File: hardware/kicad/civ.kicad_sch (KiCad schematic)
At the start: 3 parts, among them J1 CIV_3.5mm_Jack_TipRingSleeve, Q1 2N7000

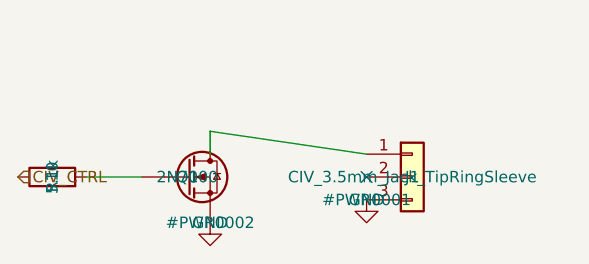
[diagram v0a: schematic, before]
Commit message: fix: repair schematic connectivity, real MAX3421E pinout, footprint assignment
- Root sheet pins were placed outside the sheet boxes, so no cross-sheet
  net (IO5->CI-V, USB D+/D-, SPI, VBUS_5V, 5V_HOST) was actually connected.
  Rebuilt pins on the sheet borders with wire stubs + labels.
- MCU: SW1/SW2 pin 2 carried both GND and EN/BOOT0 (short to ground);
  GND moved to pin 1. Unused ESP32 GPIOs marked no-connect.
- USB_Host rebuilt around the real MAX3421E TQFN-32 pinout (datasheet
  19-3953): 33 ohm D+/D- series resistors, 1uF VCC/VBCOMP, 0.1uF VL.
- J1 now AudioJack3 (T/R/S) with CUI SJ1-3523N footprint; Q1 is a real
  2N7000 (TO-92).
- PWR_FLAGs added; ERC (raw kicad-cli) has 0 errors.
- Board outline 65x45 mm, 54 footprints assigned and written to symbol
  Footprint fields, netlist applied. Placement is a rough grid only; no
  routing yet.
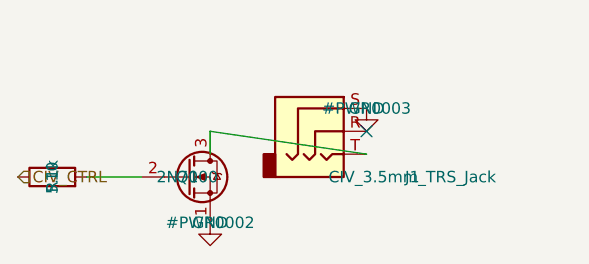
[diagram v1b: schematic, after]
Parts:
- removed J1: CIV_3.5mm_Jack_TipRingSleeve, symbol Connector_Generic:Conn_01x03
- removed Q1: 2N7000, symbol Device:Q_NMOS
- added J1: CIV_3.5mm_TRS_Jack, Connector_Audio:Jack_3.5mm_CUI_SJ1-3523N_Horizontal, symbol Connector_Audio:AudioJack3
- added Q1: 2N7000, Package_TO_SOT_THT:TO-92_Inline, symbol Transistor_FET:2N7000
- R10: footprint (none) -> Resistor_SMD:R_0603_1608Metric
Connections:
- net GND: now also J1.S, Q1.1 (S)
- net at R10.2: now also Q1.2 (G)
- new net: J1.T, Q1.3 (D)
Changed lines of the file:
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@@
 	(embedded_fonts no)
-	(symbol
-		(lib_id "Connector_Generic:Conn_01x03")
-		(at 70 110 0)
-		(unit 1)
-		(exclude_from_sim no)
-		(in_bom yes)
-		(on_board yes)
-		(dnp no)
-		(property "Reference" "J1"
-			(at 70 110 0)
-			(effects
-				(font
-					(size 1.27 1.27)
-				)
-			)
-		)
-		(property "Value" "CIV_3.5mm_Jack_TipRingSleeve"
-			(at 70 110 0)
-			(effects
-				(font
-					(size 1.27 1.27)
-				)
-			)
-		)
-		(property "Footprint" ""
-			(at 70 110 0)
-			(effects
-				(font
-					(size 1.27 1.27)
-				)
-				(hide yes)
-			)
-		)
-		(property "Datasheet" ""
-			(at 70 110 0)
-			(effects
-				(font
-					(size 1.27 1.27)
-				)
-				(hide yes)
-			)
-		)
-		(property "Description" "Generic connector, single row, 01x03, script generated (kicad-library-utils/schlib/autogen/connector/)"
-			(at 70 110 0)
-			(effects
-				(font
-					(size 1.27 1.27)
-				)
-				(hide yes)
-			)
-		)
-		(pin "1"
-		)
-		(pin "2"
-		)
-		(pin "3"
-		)
-		(instances
-			(project "WaveRig"
-				(path "/840e083b-e0fc-4c92-9ef6-5f402d7ae31c/890b54cb-1ed8-4869-b127-85ce65e524b6"
-					(reference "J1")
-					(unit 1)
-				)
-			)
-		)
-	)
-	(symbol
-		(lib_id "Device:Q_NMOS")
-		(at 45 110 0)
-		(unit 1)
-		(exclude_from_sim no)
-		(in_bom yes)
-		(on_board yes)
-		(dnp no)
-		(property "Reference" "Q1"
-			(at 45 110 0)
-			(effects
-				(font
-					(size 1.27 1.27)
-				)
-			)
-		)
-		(property "Value" "2N7000"
-			(at 45 110 0)
-			(effects
-				(font
-					(size 1.27 1.27)
-				)
-			)
-		)
-		(property "Footprint" ""
-			(at 45 110 0)
-			(effects
-				(font
-					(size 1.27 1.27)
-				)
-				(hide yes)
-			)
-		)
-		(property "Datasheet" ""
-			(at 45 110 0)
-			(effects
-				(font
-					(size 1.27 1.27)
-				)
-				(hide yes)
-			)
-		)
-		(property "Description" "N-MOSFET transistor"
-			(at 45 110 0)
-			(effects
-				(font
-					(size 1.27 1.27)
-				)
-				(hide yes)
-			)
-		)
-		(pin "D"
-		)
-		(pin "G"
-		)
-		(pin "S"
-		)
-		(instances
-			(project "WaveRig"
-				(path "/840e083b-e0fc-4c92-9ef6-5f402d7ae31c/890b54cb-1ed8-4869-b127-85ce65e524b6"
-					(reference "Q1")
-					(unit 1)
-				)
-			)
-		)
-	)
 	(symbol
 		(lib_id "Device:R")
@@
 			)
 		)
-		(property "Footprint" ""
+		(property "Footprint" "Resistor_SMD:R_0603_1608Metric"
 			(at 30 110 0)
 			(effects
@@
 			(width 0)
 			(type default)
-		)
-	)
-	(no_connect
-		(at 64.92 110)
-	)
-	(symbol
-		(lib_id "power:GND")
-		(at 64.92 112.54 0)
-		(unit 1)
-		(exclude_from_sim no)
-		(in_bom yes)
-		(on_board yes)
-		(dnp no)
-		(property "Reference" "#PWR0001"
-			(at 64.92 112.54 0)
-			(effects
-				(font
-					(size 1.27 1.27)
-				)
-			)
-		)
-		(property "Value" "GND"
-			(at 64.92 112.54 0)
-			(effects
-				(font
-					(size 1.27 1.27)
-				)
-			)
-		)
-		(property "Footprint" ""
-			(at 64.92 112.54 0)
-			(effects
-				(font
-					(size 1.27 1.27)
-				)
-				(hide yes)
-			)
-		)
-		(property "Datasheet" ""
-			(at 64.92 112.54 0)
-			(effects
-				(font
-					(size 1.27 1.27)
-				)
-				(hide yes)
-			)
-		)
-		(property "Description" "Power symbol creates a global label with name \"GND\" , ground"
-			(at 64.92 112.54 0)
-			(effects
-				(font
-					(size 1.27 1.27)
-				)
-				(hide yes)
-			)
-		)
-		(pin "1"
-		)
-		(instances
-			(project "WaveRig"
-				(path "/840e083b-e0fc-4c92-9ef6-5f402d7ae31c/890b54cb-1ed8-4869-b127-85ce65e524b6"
-					(reference "#PWR0001")
-					(unit 1)
-				)
-			)
 		)
 	)
@@
 		)
 	)
+	(symbol
+		(lib_id "Transistor_FET:2N7000")
+		(at 45 110 0)
+		(unit 1)
+		(exclude_from_sim no)
+		(in_bom yes)
+		(on_board yes)
+		(dnp no)
+		(property "Reference" "Q1"
+			(at 45 110 0)
+			(effects
+				(font
+					(size 1.27 1.27)
+				)
+			)
+		)
+		(property "Value" "2N7000"
+			(at 45 110 0)
+			(effects
+				(font
+					(size 1.27 1.27)
+				)
+			)
+		)
+		(property "Footprint" "Package_TO_SOT_THT:TO-92_Inline"
+			(at 45 110 0)
+			(effects
+				(font
+					(size 1.27 1.27)
+				)
+				(hide yes)
+			)
+		)
+		(property "Datasheet" "https://www.vishay.com/docs/70226/70226.pdf"
+			(at 45 110 0)
+			(effects
+				(font
+					(size 1.27 1.27)
+				)
+				(hide yes)
+			)
+		)
+		(property "Description" "0.2A Id, 200V Vds, N-Channel MOSFET, 2.6V Logic Level, TO-92"
+			(at 45 110 0)
+			(effects
+				(font
+					(size 1.27 1.27)
+				)
+				(hide yes)
+			)
+		)
+		(pin "1"
+		)
+		(pin "2"
+		)
+		(pin "3"
+		)
+		(instances
+			(project "WaveRig"
+				(path "/840e083b-e0fc-4c92-9ef6-5f402d7ae31c/890b54cb-1ed8-4869-b127-85ce65e524b6"
+					(reference "Q1")
+					(unit 1)
+				)
+			)
+		)
+	)
+	(symbol
+		(lib_id "Connector_Audio:AudioJack3")
+		(at 59.84 104.92 0)
+		(unit 1)
+		(exclude_from_sim no)
+		(in_bom yes)
+		(on_board yes)
+		(dnp no)
+		(property "Reference" "J1"
+			(at 70 110 0)
+			(effects
+				(font
+					(size 1.27 1.27)
+				)
+			)
+		)
+		(property "Value" "CIV_3.5mm_TRS_Jack"
+			(at 70 110 0)
+			(effects
+				(font
+					(size 1.27 1.27)
+				)
+			)
+		)
+		(property "Footprint" "Connector_Audio:Jack_3.5mm_CUI_SJ1-3523N_Horizontal"
+			(at 70 110 0)
+			(effects
+				(font
+					(size 1.27 1.27)
+				)
+				(hide yes)
+			)
+		)
+		(property "Datasheet" ""
+			(at 70 110 0)
+			(effects
+				(font
+					(size 1.27 1.27)
+				)
+				(hide yes)
+			)
+		)
+		(property "Description" "Audio Jack, 3 Poles (Stereo / TRS)"
+			(at 70 110 0)
+			(effects
+				(font
+					(size 1.27 1.27)
+				)
+				(hide yes)
+			)
+		)
+		(pin "R"
+		)
+		(pin "S"
+		)
+		(pin "T"
+		)
+		(instances
+			(project "WaveRig"
+				(path "/840e083b-e0fc-4c92-9ef6-5f402d7ae31c/890b54cb-1ed8-4869-b127-85ce65e524b6"
+					(reference "J1")
+					(unit 1)
+				)
+			)
+		)
+	)
+	(symbol
+		(lib_id "power:GND")
+		(at 64.92 102.38 0)
+		(unit 1)
+		(exclude_from_sim no)
+		(in_bom yes)
+		(on_board yes)
+		(dnp no)
+		(property "Reference" "#PWR0003"
+			(at 64.92 102.38 0)
+			(effects
+				(font
+					(size 1.27 1.27)
+				)
+			)
+		)
+		(property "Value" "GND"
+			(at 64.92 102.38 0)
+			(effects
+				(font
+					(size 1.27 1.27)
+				)
+			)
+		)
+		(property "Footprint" ""
+			(at 64.92 102.38 0)
+			(effects
+				(font
+					(size 1.27 1.27)
+				)
+				(hide yes)
+			)
+		)
+		(property "Datasheet" ""
+			(at 64.92 102.38 0)
+			(effects
+				(font
+					(size 1.27 1.27)
+				)
+				(hide yes)
+			)
+		)
+		(property "Description" "Power symbol creates a global label with name \"GND\" , ground"
+			(at 64.92 102.38 0)
+			(effects
+				(font
+					(size 1.27 1.27)
+				)
+				(hide yes)
+			)
+		)
+		(pin "1"
+		)
+		(instances
+			(project "WaveRig"
+				(path "/840e083b-e0fc-4c92-9ef6-5f402d7ae31c/890b54cb-1ed8-4869-b127-85ce65e524b6"
+					(reference "#PWR0003")
+					(unit 1)
+				)
+			)
+		)
+	)
+	(no_connect
+		(at 64.92 104.92)
+	)
 )

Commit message: fix: datasheet audit - correct charger pinout, LDO for 3V3, DW01A/FS8205A, MAX3232, CI-V RX
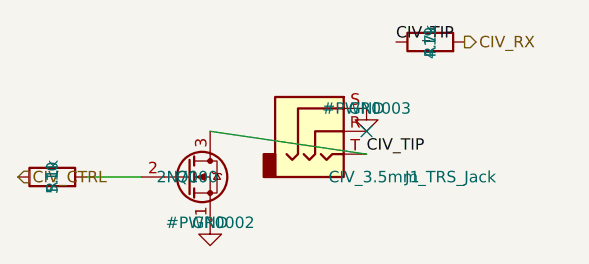
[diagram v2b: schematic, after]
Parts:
- added R19: 4.7k, Resistor_SMD:R_0603_1608Metric, symbol Device:R
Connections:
- net CIV_TIP: now reaches J1.T, Q1.3 (D)
- net CIV_TIP: now also R19.1
- new net CIV_RX: R19.2
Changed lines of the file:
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@@
-	(wire
-		(pts
-			(xy 47.54 104.92)
-			(xy 47.54 107.46)
-		)
-		(stroke
-			(width 0)
-			(type default)
-		)
-	)
 	(wire
 		(pts
@@
 		(at 64.92 104.92)
 	)
+	(symbol
+		(lib_id "Device:R")
+		(at 72 95 90)
+		(unit 1)
+		(exclude_from_sim no)
+		(in_bom yes)
+		(on_board yes)
+		(dnp no)
+		(property "Reference" "R19"
+			(at 72 95 0)
+			(effects
+				(font
+					(size 1.27 1.27)
+				)
+			)
+		)
+		(property "Value" "4.7k"
+			(at 72 95 0)
+			(effects
+				(font
+					(size 1.27 1.27)
+				)
+			)
+		)
+		(property "Footprint" "Resistor_SMD:R_0603_1608Metric"
+			(at 72 95 0)
+			(effects
+				(font
+					(size 1.27 1.27)
+				)
+				(hide yes)
+			)
+		)
+		(property "Datasheet" ""
+			(at 72 95 0)
+			(effects
+				(font
+					(size 1.27 1.27)
+				)
+				(hide yes)
+			)
+		)
+		(property "Description" "Resistor"
+			(at 72 95 0)
+			(effects
+				(font
+					(size 1.27 1.27)
+				)
+				(hide yes)
+			)
+		)
+		(pin "1"
+		)
+		(pin "2"
+		)
+		(instances
+			(project "WaveRig"
+				(path "/840e083b-e0fc-4c92-9ef6-5f402d7ae31c/890b54cb-1ed8-4869-b127-85ce65e524b6"
+					(reference "R19")
+					(unit 1)
+				)
+			)
+		)
+	)
+	(label "CIV_TIP"
+		(at 64.92 107.46 0)
+		(effects
+			(font
+				(size 1.27 1.27)
+			)
+			(justify left bottom)
+		)
+	)
+	(label "CIV_TIP"
+		(at 68.19 95 0)
+		(effects
+			(font
+				(size 1.27 1.27)
+			)
+			(justify left bottom)
+		)
+	)
+	(hierarchical_label "CIV_RX"
+		(shape output)
+		(at 75.81 95 0)
+		(effects
+			(font
+				(size 1.27 1.27)
+			)
+			(justify left)
+		)
+	)
 )
